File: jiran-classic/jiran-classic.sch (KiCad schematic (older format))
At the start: 132 parts, among them J1 TRRS, Q1 2N7002, SW1 SW_Push, SW10 SW_Push, SW11 SW_Push, SW12 SW_Push, SW13 SW_Push, SW14 SW_Push, SW15 SW_Push, SW16 SW_Push, SW17 SW_Push, SW18 SW_Push, SW19 SW_Push, SW2 SW_Push, SW20 SW_Push, SW21 SW_Push, SW22 SW_Push, SW23 SW_Push, SW24 SW_Push, SW25 SW_Push, SW26 SW_Push, SW27 SW_Push, SW28 SW_Push, SW29 SW_Push, SW3 SW_Push, SW4 SW_Push, SW5 SW_Push, SW6 SW_Push, SW7 SW_Push, SW8 SW_Push, SW9 SW_Push, U1 ProMicro

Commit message: Rename files
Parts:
- G1, G2: symbol jiran:LOGO -> jiran-classic-rescue:LOGO-jiran
- J1: symbol Pcb-rescue:MJ-4PP-9-kbd -> jiran-classic-rescue:MJ-4PP-9-kbd-Pcb-rescue
- U1: symbol Pcb-rescue:ProMicro-kbd -> jiran-classic-rescue:ProMicro-kbd-Pcb-rescue
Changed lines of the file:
@@
 $EndComp
 $Comp
-L Pcb-rescue:MJ-4PP-9-kbd J1
+L jiran-classic-rescue:MJ-4PP-9-kbd-Pcb-rescue J1
 U 1 1 5DBFACF7
 P 955 2900
@@
 Connection ~ 1240 1145
 $Comp
-L Pcb-rescue:ProMicro-kbd U1
+L jiran-classic-rescue:ProMicro-kbd-Pcb-rescue U1
 U 1 1 5DAA926E
 P 1940 1695
@@
 	9360 1785 9360 2285
 $Comp
-L jiran:LOGO G1
+L jiran-classic-rescue:LOGO-jiran G1
 U 1 1 5FA09AD8
 P 8900 4250
@@
 $EndComp
 $Comp
-L jiran:LOGO G2
+L jiran-classic-rescue:LOGO-jiran G2
 U 1 1 5FA0B668
 P 9350 4250

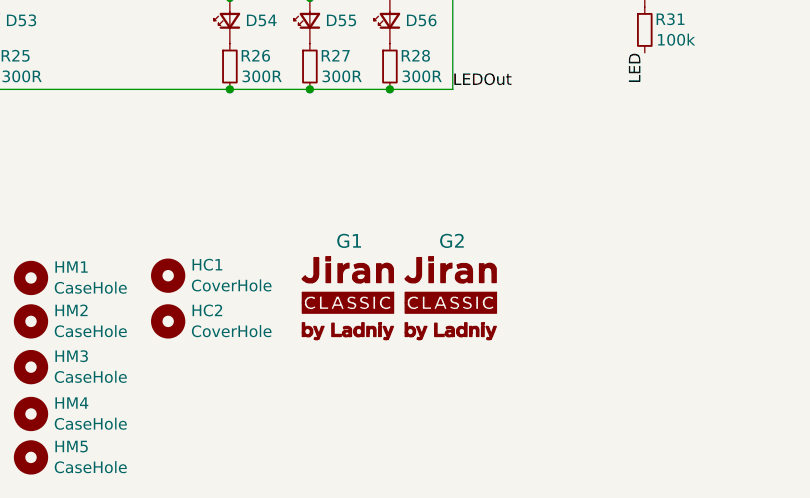
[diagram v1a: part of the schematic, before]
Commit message: Update logo symbol
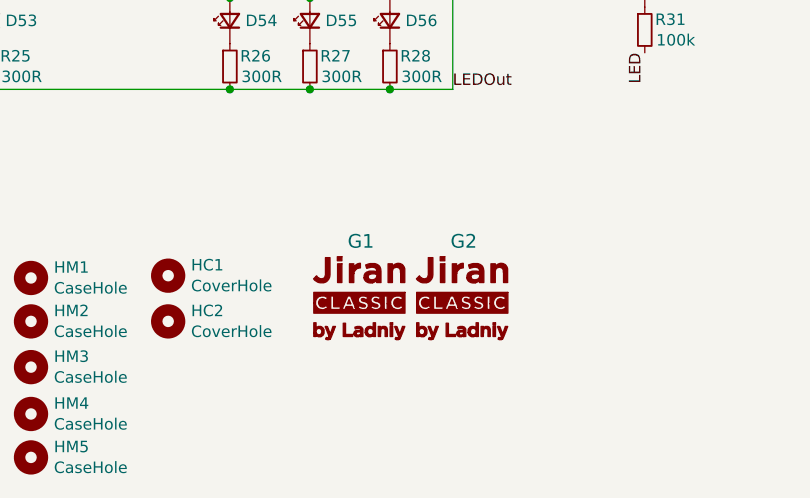
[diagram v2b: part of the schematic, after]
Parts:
- removed G1, G2: LOGO, used_footprints:Silk_Logotype, symbol jiran-classic-rescue:LOGO-jiran
- added G1, G2: logo-jiran-classic, used_footprints:Silk_Logo_Classic, symbol jiran:logo-jiran-classic
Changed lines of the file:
@@
 	9360 1785 9360 2285
 $Comp
-L jiran-classic-rescue:LOGO-jiran G1
-U 1 1 5FA09AD8
-P 8900 4250
-F 0 "G1" H 8850 4550 60  0000 L CNN
-F 1 "LOGO" H 8900 4050 60  0001 C CNN
-F 2 "used_footprints:Silk_Logotype" H 8900 4250 50  0001 C CNN
-F 3 "" H 8900 4250 50  0001 C CNN
-	1    8900 4250
+L jiran:logo-jiran-classic G1
+U 1 1 5FA0EF82
+P 8950 4200
+F 0 "G1" H 8900 4450 60  0000 L CNN
+F 1 "logo-jiran-classic" H 8950 3950 60  0001 C CNN
+F 2 "used_footprints:Silk_Logo_Classic" H 8950 4200 50  0001 C CNN
+F 3 "" H 8950 4200 50  0001 C CNN
+	1    8950 4200
 	1    0    0    -1
 $EndComp
 $Comp
-L jiran-classic-rescue:LOGO-jiran G2
-U 1 1 5FA0B668
-P 9350 4250
-F 0 "G2" H 9300 4550 60  0000 L CNN
-F 1 "LOGO" H 9350 4050 60  0001 C CNN
-F 2 "used_footprints:Silk_Logotype" H 9350 4250 50  0001 C CNN
-F 3 "" H 9350 4250 50  0001 C CNN
-	1    9350 4250
+L jiran:logo-jiran-classic G2
+U 1 1 5FA104C5
+P 9400 4200
+F 0 "G2" H 9350 4450 60  0000 L CNN
+F 1 "logo-jiran-classic" H 9400 3950 60  0001 C CNN
+F 2 "used_footprints:Silk_Logo_Classic" H 9400 4200 50  0001 C CNN
+F 3 "" H 9400 4200 50  0001 C CNN
+	1    9400 4200
 	1    0    0    -1
 $EndComp
